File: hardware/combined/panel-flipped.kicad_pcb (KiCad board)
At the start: 2 copper layers, 62 x 104.3 mm, 5 parts

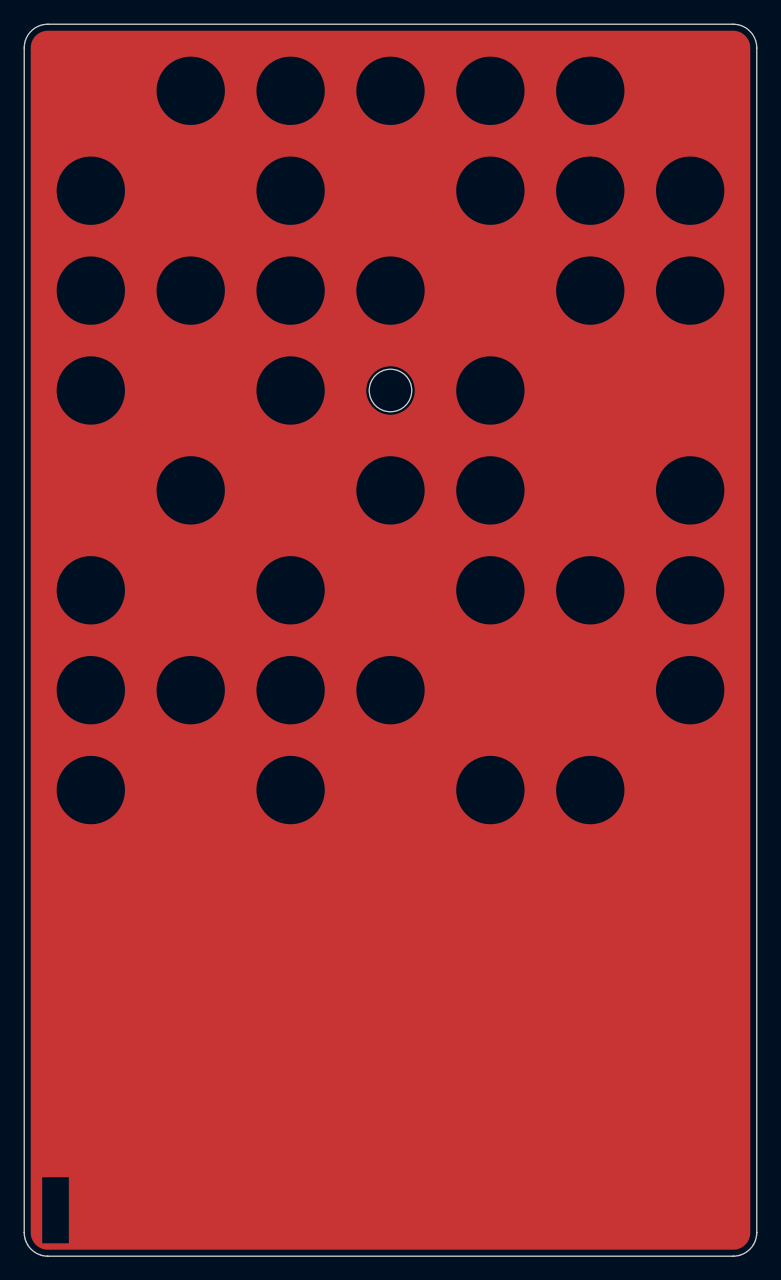
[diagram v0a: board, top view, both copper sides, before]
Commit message: Panel: test hole 3.6 -> 3.8mm for the TS-1002's 3.5+/-0.2mm shaft
Datasheet-verified: the switch is 16.0mm tall (correct for 0.5-1mm proud at
a 13.4-13.9mm lattice) but its shaft is 3.5mm — 3.6 left 0.05mm/side and a
tolerance-stack bind. Wells chose the bigger hole over a printed plunger.
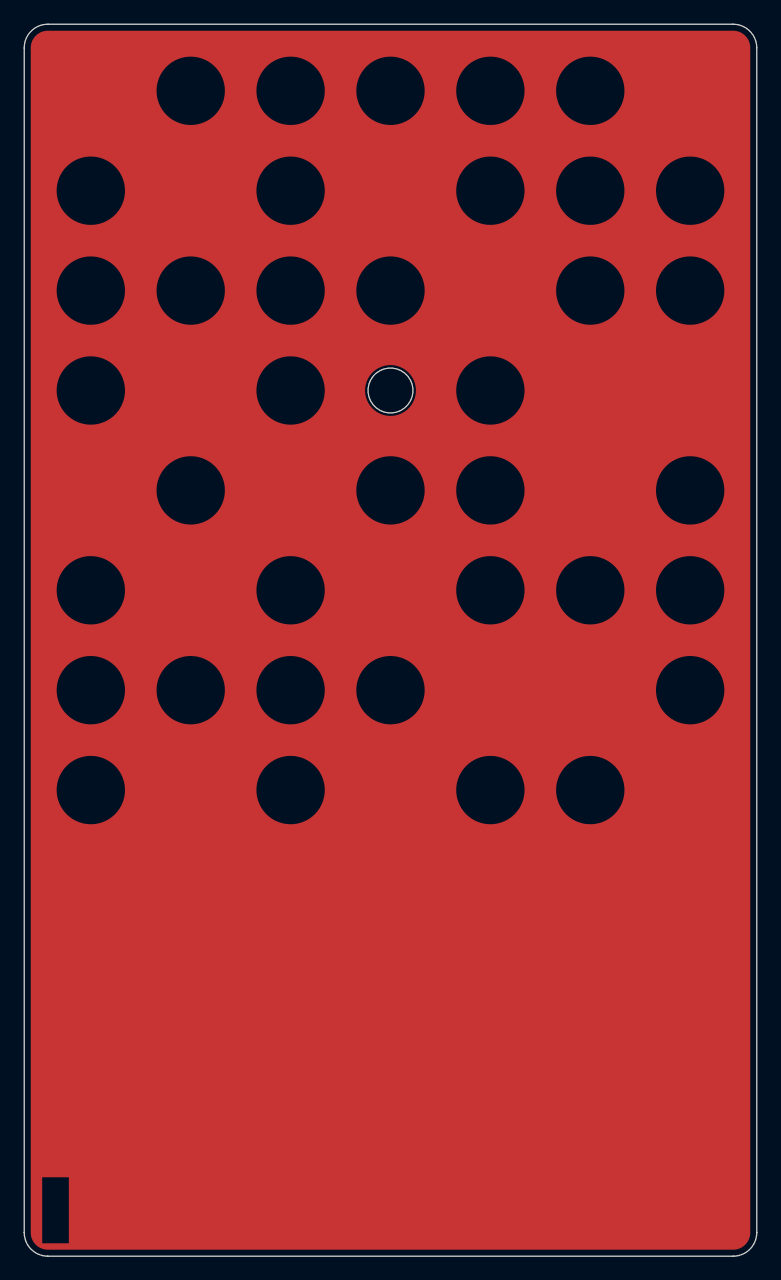
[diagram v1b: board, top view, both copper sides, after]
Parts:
- moved MT1 50.7 mm to (56.4, 5.64)
- moved MT2 50.7 mm to (5.64, 5.64)
- moved MT3 47.7 mm to (56.4, 91.9)
- moved MT4 47.7 mm to (8.64, 91.9)
- renumbered MT2 to MT1, MT1 to MT2, MT4 to MT3, MT3 to MT4

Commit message: Panel: Frame 26 test dot — squared gold tab, glyphs clear of the 3.8mm hole
Wells redrew the test dot for the bigger hole: gold teardrop (disc + rounded
SE tab), hole marker at 3.83mm, 'test' knockout letters moved onto the tab.
Generator changes to carry it: knockout ownership reach 1.45r (glyphs live
past the disc edge now), glyph subtraction by boolean (edge-crossing holes
voided the whole opening), gold copper clipped around the NPTH, gold-art
mask opening keeps mask over knockout strokes.
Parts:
- moved MT1 98.6 mm to (56.4, 5.64)
- moved MT4 98.6 mm to (8.64, 91.9)
- renumbered MT4 to MT1, MT1 to MT4

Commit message: Panel: black ring around the test hole + repositioned glyphs (Frame 26 rev 2)
Mask now stays closed inside the black marker circle (3.83mm), so the
drill's surround reads black instead of a bare-FR4 cream ring; marker
diameter rides in panel_layout.json as hole_mark_dia. Wells's updated
export pulls the glyphs 3px left so the final t clears the tab edge.
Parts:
- moved MT1 98.6 mm to (56.4, 5.64)
- moved MT3 86.3 mm to (56.4, 91.9)
- moved MT4 47.7 mm to (8.64, 91.9)
- renumbered MT4 to MT1, MT1 to MT3, MT3 to MT4

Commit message: Regenerate fab outputs after the mask-edge revert
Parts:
- moved MT1 98.6 mm to (56.4, 5.64)
- moved MT4 98.6 mm to (8.64, 91.9)
- renumbered MT4 to MT1, MT1 to MT4
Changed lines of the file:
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@@
 	(footprint "panel:SMT_Standoff_M2.5_D6.0mm"
 		(layer "F.Cu")
-		(at 56.3636 5.6364 180)
-		(property "Reference" "MT1"
+		(at 8.6364 91.93 180)
+		(property "Reference" "MT4"
 			(at 0 0 0)
 			(layer "B.SilkS")
@@
 	(footprint "panel:SMT_Standoff_M2.5_D6.0mm"
 		(layer "F.Cu")
-		(at 8.6364 91.93 180)
-		(property "Reference" "MT4"
+		(at 56.3636 5.6364 180)
+		(property "Reference" "MT1"
 			(at 0 0 0)
 			(layer "B.SilkS")

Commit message: Regenerate panel, combined panel and fab packages
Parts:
- moved MT2 100.1 mm to (5.64, 5.64)
- moved MT3 100.1 mm to (56.4, 91.9)
- renumbered MT3 to MT2, MT2 to MT3
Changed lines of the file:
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@@
 	(footprint "panel:SMT_Standoff_M2.5_D6.0mm"
 		(layer "F.Cu")
-		(at 5.6364 5.6364 180)
-		(property "Reference" "MT2"
+		(at 56.3636 91.93 180)
+		(property "Reference" "MT3"
 			(at 0 0 0)
 			(layer "B.SilkS")
@@
 	(footprint "panel:SMT_Standoff_M2.5_D6.0mm"
 		(layer "F.Cu")
-		(at 56.3636 91.93 180)
-		(property "Reference" "MT3"
-			(at 0 0 0)
-			(layer "B.SilkS")
+		(at 5.6364 5.6364 180)
+		(property "Reference" "MT2"
+			(at 0 0 0)
+			(layer "B.SilkS")

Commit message: Pre-order review #2: stitch 10 stranded GND islands, H4 and VBUS via fixes, CAM-clean seam, CTS invert option
Ten top-side GND islands (SP3490, both SP3485 grounds, LED 20 onward, the WROOM's
100 nF caps, CC1's pulldown, SP3232 V+ cap and T2IN tie) had no via to the plane.
KiCad reported them as Zone<->Zone unconnected items and the 08-22 review had
classed those as benign. Twelve vias and three short bottom-side jogs (VBUS trunk
by U1, 3V3 diagonal and VBUS via at H4, DIP5 diagonal by U3) bring the GND net
to one cluster; DRC is 0 errors / 0 unconnected with schematic parity.

Also: second via on the 5 V layer crossing by U1/D10; V-CUT score line and label
moved from Edge.Cuts to User.Comments; H_TEST excluded from pos/BOM; make_fab.sh
regenerates the PCBWay package; firmware gains CONFIG_AIRWRITER_INVERT_CTS and the
serial_out CTS comment now matches the code. Report: docs/review-2026-08-25-pre-order-2.md
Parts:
- moved MT2 100.1 mm to (5.64, 5.64)
- moved MT1 98.6 mm to (56.4, 5.64)
- moved MT4 86.3 mm to (8.64, 91.9)
- moved MT3 86.3 mm to (56.4, 91.9)
- renumbered MT4 to MT1, MT3 to MT2, MT1 to MT3, MT2 to MT4
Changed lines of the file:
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@@
+	(footprint "panel:SMT_Standoff_M2.5_D6.0mm"
+		(layer "F.Cu")
+		(at 5.6364 5.6364 180)
+		(property "Reference" "MT2"
+			(at 0 0 0)
+			(layer "B.SilkS")
+			(hide yes)
+			(effects
+				(font
+					(size 1.27 1.27)
+				)
+				(justify mirror)
+			)
+		)
+		(property "Value" "9774030151R"
+			(at 0 0 0)
+			(layer "B.Fab")
+			(hide yes)
+			(effects
+				(font
+					(size 1.27 1.27)
+				)
+				(justify mirror)
+			)
+		)
+		(property "Datasheet" ""
+			(at 0 0 0)
+			(layer "B.Fab")
+			(hide yes)
+			(effects
+				(font
+					(size 1.27 1.27)
+				)
+				(justify mirror)
+			)
+		)
+		(property "Description" ""
+			(at 0 0 0)
+			(layer "B.Fab")
+			(hide yes)
+			(effects
+				(font
+					(size 1.27 1.27)
+				)
+				(justify mirror)
+			)
+		)
+		(attr smd)
+		(duplicate_pad_numbers_are_jumpers no)
+		(pad "" smd circle
+			(at 0 0 180)
+			(size 6 6)
+			(layers "F.Mask")
+		)
+		(embedded_fonts no)
+		(model "${KICAD10_3DMODEL_DIR}/Mounting_Wuerth.3dshapes/Mounting_Wuerth_WA-SMSI-M2.5_H3mm_9774030151.step"
+			(offset
+				(xyz 0 0 0)
+			)
+			(scale
+				(xyz 1 1 1)
+			)
+			(rotate
+				(xyz 0 0 0)
+			)
+		)
+	)
+	(footprint "panel:SMT_Standoff_M2.5_D6.0mm"
+		(layer "F.Cu")
+		(at 56.3636 5.6364 180)
+		(property "Reference" "MT1"
+			(at 0 0 0)
+			(layer "B.SilkS")
+			(hide yes)
+			(effects
+				(font
+					(size 1.27 1.27)
+				)
+				(justify mirror)
+			)
+		)
+		(property "Value" "9774030151R"
+			(at 0 0 0)
+			(layer "B.Fab")
+			(hide yes)
+			(effects
+				(font
+					(size 1.27 1.27)
+				)
+				(justify mirror)
+			)
+		)
+		(property "Datasheet" ""
+			(at 0 0 0)
+			(layer "B.Fab")
+			(hide yes)
+			(effects
+				(font
+					(size 1.27 1.27)
+				)
+				(justify mirror)
+			)
+		)
+		(property "Description" ""
+			(at 0 0 0)
+			(layer "B.Fab")
+			(hide yes)
+			(effects
+				(font
+					(size 1.27 1.27)
+				)
+				(justify mirror)
+			)
+		)
+		(attr smd)
+		(duplicate_pad_numbers_are_jumpers no)
+		(pad "" smd circle
+			(at 0 0 180)
+			(size 6 6)
+			(layers "F.Mask")
+		)
+		(embedded_fonts no)
+		(model "${KICAD10_3DMODEL_DIR}/Mounting_Wuerth.3dshapes/Mounting_Wuerth_WA-SMSI-M2.5_H3mm_9774030151.step"
+			(offset
+				(xyz 0 0 0)
+			)
+			(scale
+				(xyz 1 1 1)
+			)
+			(rotate
+				(xyz 0 0 0)
+			)
+		)
+	)
 	(footprint "panel:SMT_Standoff_M2.5_D6.0mm"
 		(layer "F.Cu")
@@
 		)
 	)
-	(footprint "panel:SMT_Standoff_M2.5_D6.0mm"
-		(layer "F.Cu")
-		(at 56.3636 5.6364 180)
-		(property "Reference" "MT1"
-			(at 0 0 0)
-			(layer "B.SilkS")
-			(hide yes)
-			(effects
-				(font
-					(size 1.27 1.27)
-				)
-				(justify mirror)
-			)
-		)
-		(property "Value" "9774030151R"
-			(at 0 0 0)
-			(layer "B.Fab")
-			(hide yes)
-			(effects
-				(font
-					(size 1.27 1.27)
-				)
-				(justify mirror)
-			)
-		)
-		(property "Datasheet" ""
-			(at 0 0 0)
-			(layer "B.Fab")
-			(hide yes)
-			(effects
-				(font
-					(size 1.27 1.27)
-				)
-				(justify mirror)
-			)
-		)
-		(property "Description" ""
-			(at 0 0 0)
-			(layer "B.Fab")
-			(hide yes)
-			(effects
-				(font
-					(size 1.27 1.27)
-				)
-				(justify mirror)
-			)
-		)
-		(attr smd)
-		(duplicate_pad_numbers_are_jumpers no)
-		(pad "" smd circle
-			(at 0 0 180)
-			(size 6 6)
-			(layers "F.Mask")
-		)
-		(embedded_fonts no)
-		(model "${KICAD10_3DMODEL_DIR}/Mounting_Wuerth.3dshapes/Mounting_Wuerth_WA-SMSI-M2.5_H3mm_9774030151.step"
-			(offset
-				(xyz 0 0 0)
-			)
-			(scale
-				(xyz 1 1 1)
-			)
-			(rotate
-				(xyz 0 0 0)
-			)
-		)
-	)
-	(footprint "panel:SMT_Standoff_M2.5_D6.0mm"
-		(layer "F.Cu")
-		(at 5.6364 5.6364 180)
-		(property "Reference" "MT2"
-			(at 0 0 0)
-			(layer "B.SilkS")
-			(hide yes)
-			(effects
-				(font
-					(size 1.27 1.27)
-				)
-				(justify mirror)
-			)
-		)
-		(property "Value" "9774030151R"
-			(at 0 0 0)
-			(layer "B.Fab")
-			(hide yes)
-			(effects
-				(font
-					(size 1.27 1.27)
-				)
-				(justify mirror)
-			)
-		)
-		(property "Datasheet" ""
-			(at 0 0 0)
-			(layer "B.Fab")
-			(hide yes)
-			(effects
-				(font
-					(size 1.27 1.27)
-				)
-				(justify mirror)
-			)
-		)
-		(property "Description" ""
-			(at 0 0 0)
-			(layer "B.Fab")
-			(hide yes)
-			(effects
-				(font
-					(size 1.27 1.27)
-				)
-				(justify mirror)
-			)
-		)
-		(attr smd)
-		(duplicate_pad_numbers_are_jumpers no)
-		(pad "" smd circle
-			(at 0 0 180)
-			(size 6 6)
-			(layers "F.Mask")
-		)
-		(embedded_fonts no)
-		(model "${KICAD10_3DMODEL_DIR}/Mounting_Wuerth.3dshapes/Mounting_Wuerth_WA-SMSI-M2.5_H3mm_9774030151.step"
-			(offset
-				(xyz 0 0 0)
-			)
-			(scale
-				(xyz 1 1 1)
-			)
-			(rotate
-				(xyz 0 0 0)
-			)
-		)
-	)
 	(footprint ""
 		(layer "B.Cu")
@@
 			)
 		)
+		(attr exclude_from_pos_files exclude_from_bom)
 		(duplicate_pad_numbers_are_jumpers no)
 		(pad "" np_thru_hole circle

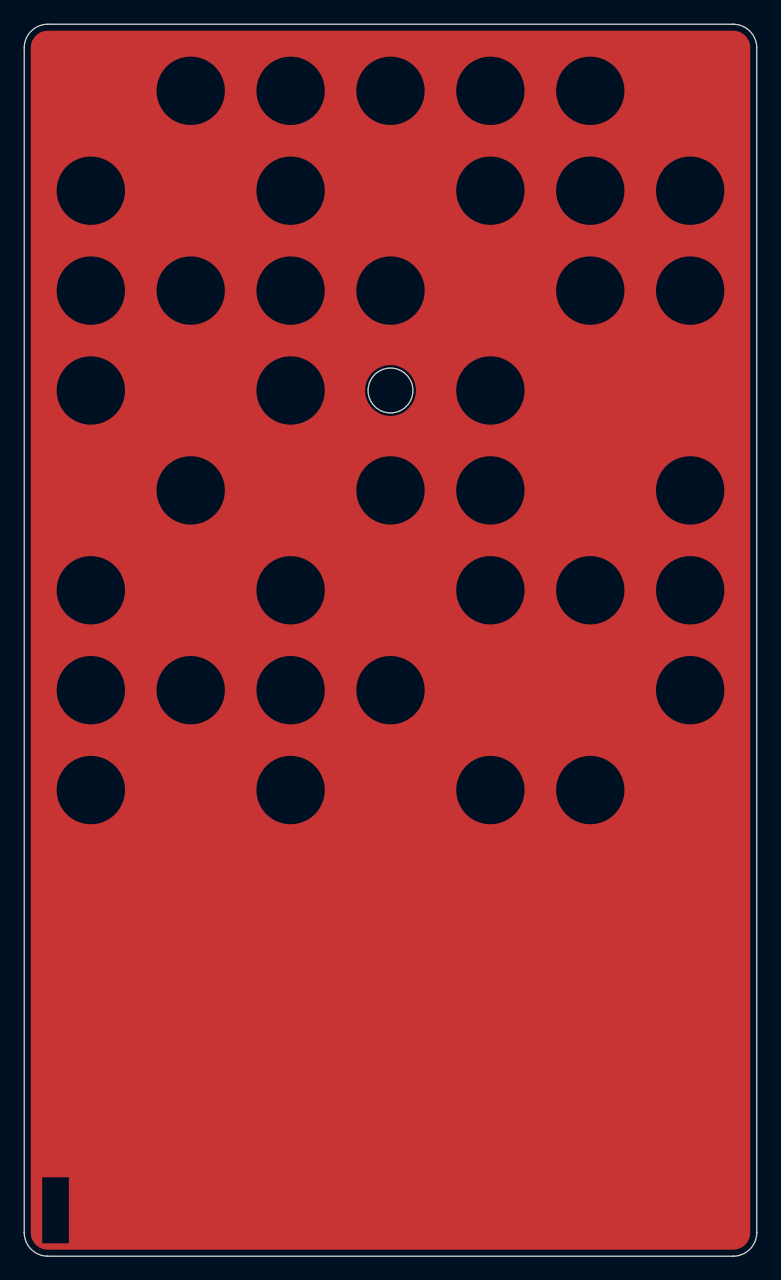
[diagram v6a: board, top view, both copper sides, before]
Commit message: Panel: plate the test hole — gold to the bore, no black surround
The 3.8mm test hole becomes a plated pad (O4.4 pad, copper layers only):
the bore wall takes ENIG and reads gold, the keep_dia black surround and
its sub-0.1mm mask sliver are gone, and mask opens to the drill edge.
Pad + annulus ring + tab art share decorative net PANEL_AU so their
contact doesn't DRC as a short; combine_boards.py carries that one net
through and strips all others (a pad's stripped (net 0) doesn't parse -
delete the node instead). Flood window grown to clear the pad by 0.25mm.
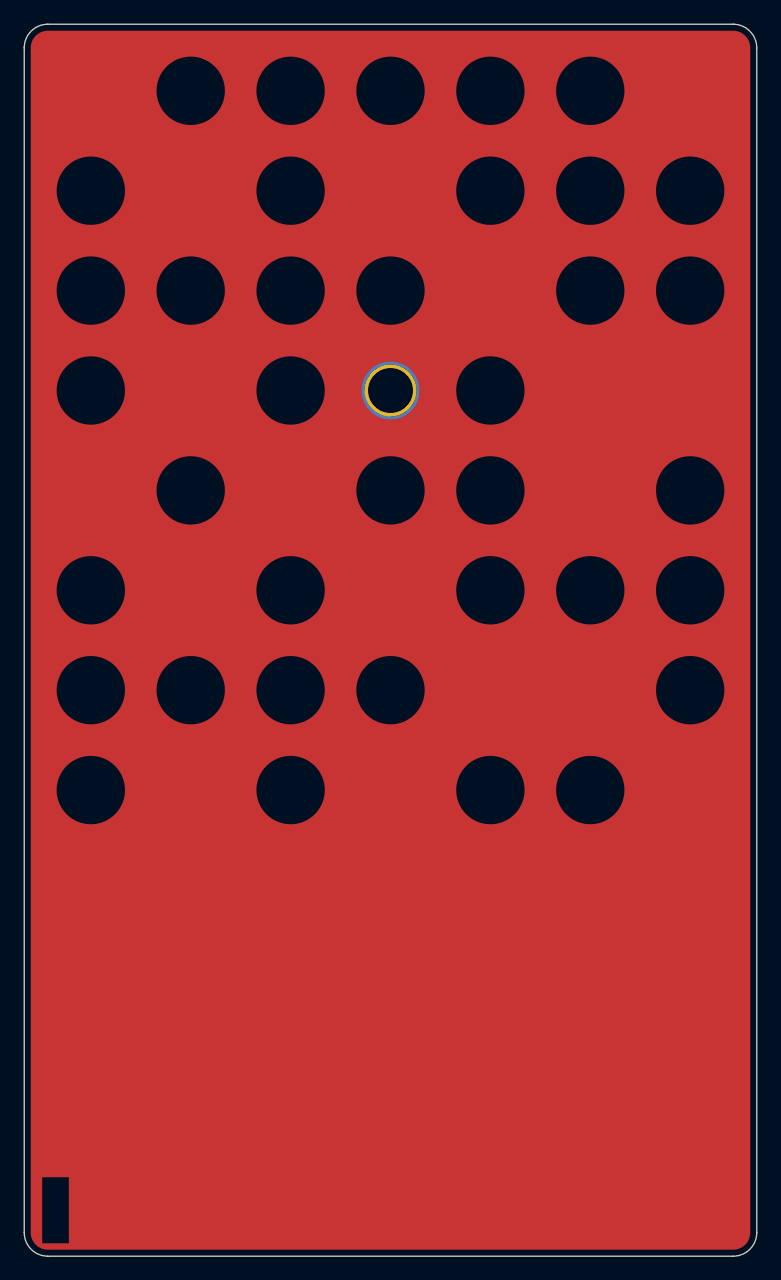
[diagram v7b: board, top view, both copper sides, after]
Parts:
- moved MT3 100.1 mm to (56.4, 91.9)
- moved MT4 98.6 mm to (8.64, 91.9)
- moved MT2 86.3 mm to (5.64, 5.64)
- moved MT1 86.3 mm to (56.4, 5.64)
- renumbered MT3 to MT1, MT4 to MT2, MT2 to MT3, MT1 to MT4
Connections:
- H_TEST pad : (no net) -> PANEL_AU

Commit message: Panel: swap too-small test label for a dot mark (PCBWay EQ)
PCBWay flagged the "test" soldermask label on the cover panel as below
their minimum feature size. Frame 9 drops that four-glyph label and adds a
~0.9mm accent dot in the test cell's lobe, with the lobe corner radius
opened from 10u to 12u.

The dot is emitted as a #111111 mask-knockout path -- the panel pipeline
ignores <circle> and only ingests white/#fff/#111 fills, so a plain black
circle would have been silently dropped. As a knockout it renders as a
kept-soldermask island on exposed gold. Regenerated panel -> combined ->
fab. Smallest B_Mask features in that cell: 0.90mm island, 0.23mm opening.
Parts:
- moved MT2 100.1 mm to (5.64, 5.64)
- moved MT3 100.1 mm to (56.4, 91.9)
- renumbered MT3 to MT2, MT2 to MT3
